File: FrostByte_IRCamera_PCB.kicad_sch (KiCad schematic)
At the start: 0 parts

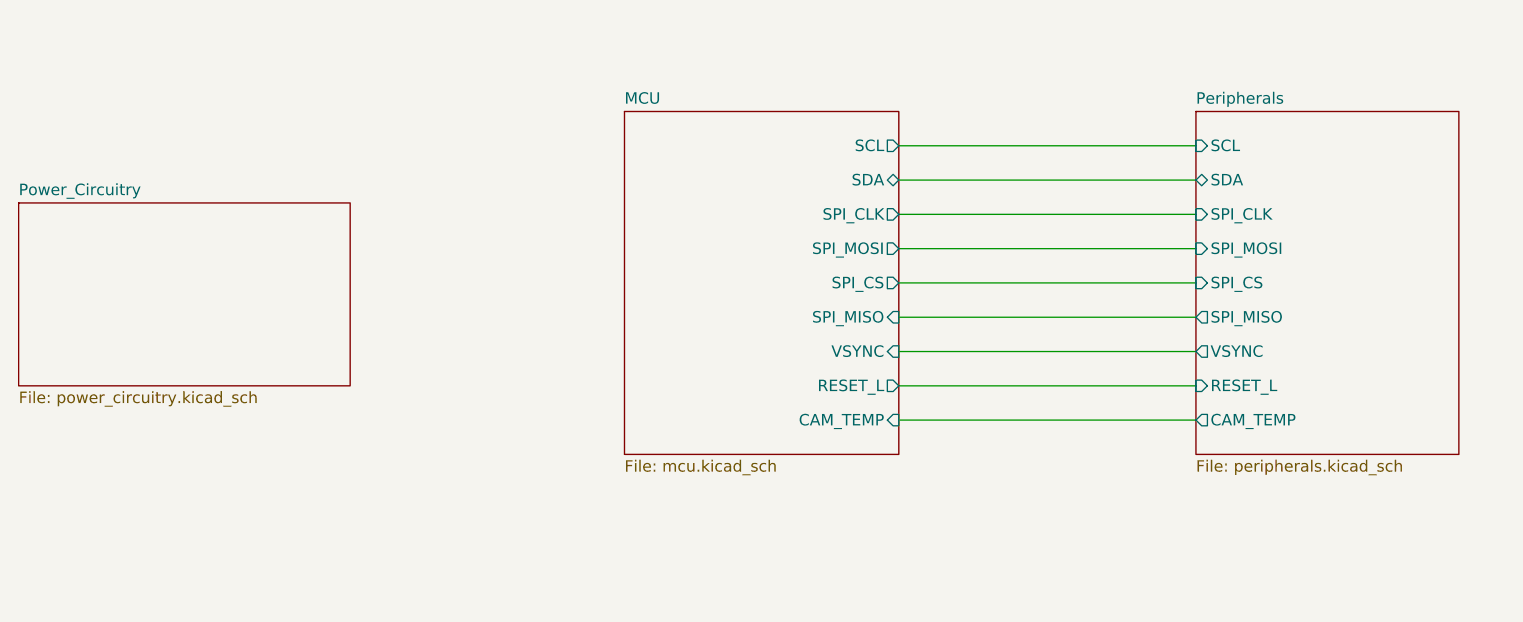
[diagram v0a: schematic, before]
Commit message: rev 2 added usb prog and i2c level shifting
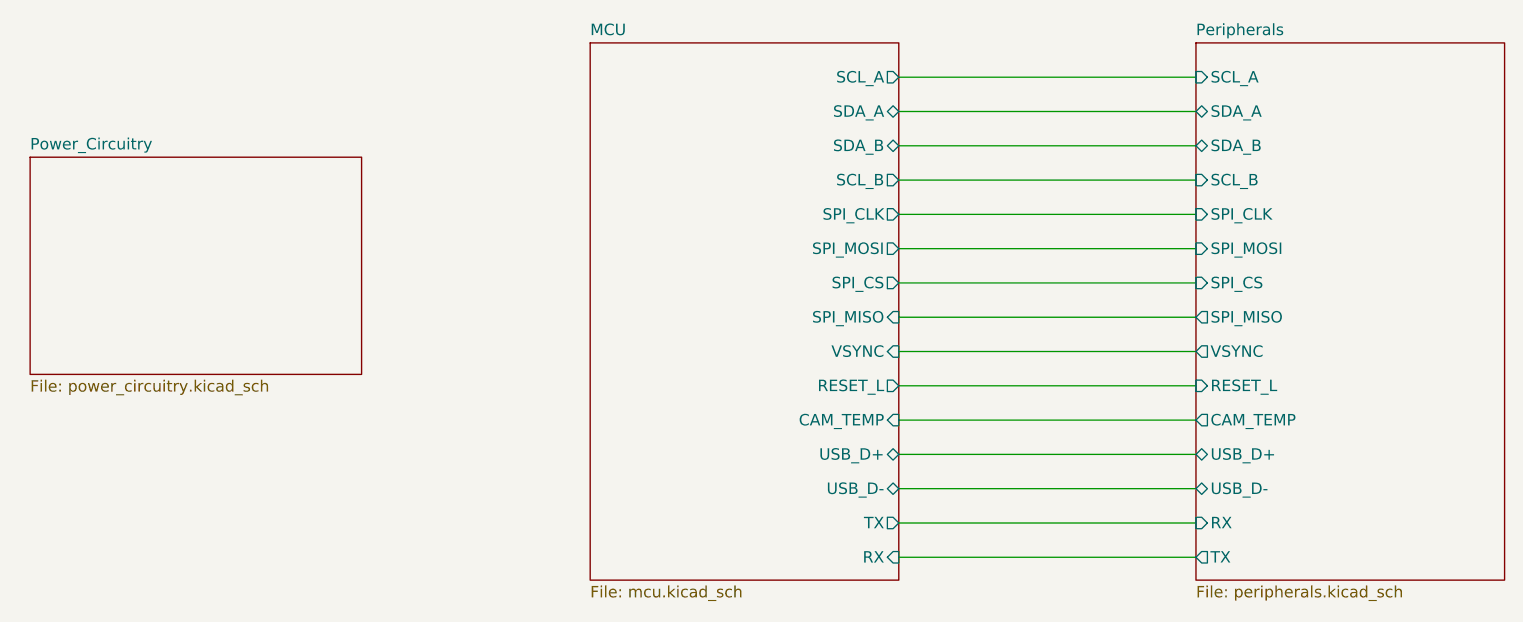
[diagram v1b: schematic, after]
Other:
- sheet MCU ports: added RX, SCL_A, SCL_B, SDA_A, SDA_B, TX, USB_D+, USB_D-; removed SCL, SDA
- sheet Peripherals ports: added RX, SCL_A, SCL_B, SDA_A, SDA_B, TX, USB_D+, USB_D-; removed SCL, SDA
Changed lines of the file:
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@@
+	(wire
+		(pts
+			(xy 162.56 76.2) (xy 195.58 76.2)
+		)
+		(stroke
+			(width 0)
+			(type default)
+		)
+	)
 	(wire
 		(pts
@@
 	(wire
 		(pts
+			(xy 162.56 114.3) (xy 195.58 114.3)
+		)
+		(stroke
+			(width 0)
+			(type default)
+		)
+	)
+	(wire
+		(pts
+			(xy 162.56 72.39) (xy 195.58 72.39)
+		)
+		(stroke
+			(width 0)
+			(type default)
+		)
+	)
+	(wire
+		(pts
 			(xy 162.56 87.63) (xy 195.58 87.63)
 		)
@@
 	(wire
 		(pts
+			(xy 162.56 125.73) (xy 195.58 125.73)
+		)
+		(stroke
+			(width 0)
+			(type default)
+		)
+	)
+	(wire
+		(pts
 			(xy 162.56 95.25) (xy 195.58 95.25)
 		)
@@
 		)
 	)
+	(wire
+		(pts
+			(xy 162.56 121.92) (xy 195.58 121.92)
+		)
+		(stroke
+			(width 0)
+			(type default)
+		)
+	)
+	(wire
+		(pts
+			(xy 162.56 118.11) (xy 195.58 118.11)
+		)
+		(stroke
+			(width 0)
+			(type default)
+		)
+	)
 	(sheet
-		(at 132.08 76.2)
-		(size 30.48 38.1)
+		(at 128.27 68.58)
+		(size 34.29 59.69)
 		(fields_autoplaced yes)
 		(stroke
@@
 		)
 		(property "Sheetname" "MCU"
-			(at 132.08 75.4884 0)
+			(at 128.27 67.8684 0)
 			(effects
 				(font
@@
 		)
 		(property "Sheetfile" "mcu.kicad_sch"
-			(at 132.08 114.8846 0)
+			(at 128.27 128.8546 0)
 			(effects
 				(font
@@
 			)
 		)
-		(pin "SCL" output
-			(at 162.56 80.01 0)
-			(effects
-				(font
-					(size 1.27 1.27)
-				)
-				(justify right)
-			)
-		)
-		(pin "SDA" bidirectional
-			(at 162.56 83.82 0)
-			(effects
-				(font
-					(size 1.27 1.27)
-				)
-				(justify right)
-			)
-		)
 		(pin "VSYNC" input
 			(at 162.56 102.87 0)
@@
 		(pin "SPI_MISO" input
 			(at 162.56 99.06 0)
+			(effects
+				(font
+					(size 1.27 1.27)
+				)
+				(justify right)
+			)
+		)
+		(pin "SCL_A" output
+			(at 162.56 72.39 0)
+			(effects
+				(font
+					(size 1.27 1.27)
+				)
+				(justify right)
+			)
+		)
+		(pin "SDA_A" bidirectional
+			(at 162.56 76.2 0)
+			(effects
+				(font
+					(size 1.27 1.27)
+				)
+				(justify right)
+			)
+		)
+		(pin "SDA_B" bidirectional
+			(at 162.56 80.01 0)
+			(effects
+				(font
+					(size 1.27 1.27)
+				)
+				(justify right)
+			)
+		)
+		(pin "SCL_B" output
+			(at 162.56 83.82 0)
+			(effects
+				(font
+					(size 1.27 1.27)
+				)
+				(justify right)
+			)
+		)
+		(pin "USB_D-" bidirectional
+			(at 162.56 118.11 0)
+			(effects
+				(font
+					(size 1.27 1.27)
+				)
+				(justify right)
+			)
+		)
+		(pin "USB_D+" bidirectional
+			(at 162.56 114.3 0)
+			(effects
+				(font
+					(size 1.27 1.27)
+				)
+				(justify right)
+			)
+		)
+		(pin "TX" output
+			(at 162.56 121.92 0)
+			(effects
+				(font
+					(size 1.27 1.27)
+				)
+				(justify right)
+			)
+		)
+		(pin "RX" input
+			(at 162.56 125.73 0)
 			(effects
 				(font
@@
 	)
 	(sheet
-		(at 195.58 76.2)
-		(size 29.21 38.1)
+		(at 195.58 68.58)
+		(size 34.29 59.69)
 		(fields_autoplaced yes)
 		(stroke
@@
 		)
 		(property "Sheetname" "Peripherals"
-			(at 195.58 75.4884 0)
+			(at 195.58 67.8684 0)
 			(effects
 				(font
@@
 		)
 		(property "Sheetfile" "peripherals.kicad_sch"
-			(at 195.58 114.8846 0)
+			(at 195.58 128.8546 0)
 			(effects
 				(font
@@
 			)
 		)
-		(pin "SCL" input
+		(pin "SCL_B" input
+			(at 195.58 83.82 180)
+			(effects
+				(font
+					(size 1.27 1.27)
+				)
+				(justify left)
+			)
+		)
+		(pin "SDA_B" bidirectional
 			(at 195.58 80.01 180)
 			(effects
@@
 			)
 		)
-		(pin "SDA" bidirectional
-			(at 195.58 83.82 180)
+		(pin "SCL_A" input
+			(at 195.58 72.39 180)
+			(effects
+				(font
+					(size 1.27 1.27)
+				)
+				(justify left)
+			)
+		)
+		(pin "SDA_A" bidirectional
+			(at 195.58 76.2 180)
+			(effects
+				(font
+					(size 1.27 1.27)
+				)
+				(justify left)
+			)
+		)
+		(pin "USB_D-" bidirectional
+			(at 195.58 118.11 180)
+			(effects
+				(font
+					(size 1.27 1.27)
+				)
+				(justify left)
+			)
+		)
+		(pin "USB_D+" bidirectional
+			(at 195.58 114.3 180)
+			(effects
+				(font
+					(size 1.27 1.27)
+				)
+				(justify left)
+			)
+		)
+		(pin "RX" input
+			(at 195.58 121.92 180)
+			(effects
+				(font
+					(size 1.27 1.27)
+				)
+				(justify left)
+			)
+		)
+		(pin "TX" output
+			(at 195.58 125.73 180)
 			(effects
 				(font
@@
 	)
 	(sheet
-		(at 64.77 86.36)
-		(size 36.83 20.32)
+		(at 66.04 81.28)
+		(size 36.83 24.13)
 		(fields_autoplaced yes)
 		(stroke
@@
 		)
 		(property "Sheetname" "Power_Circuitry"
-			(at 64.77 85.6484 0)
+			(at 66.04 80.5684 0)
 			(effects
 				(font
@@
 		)
 		(property "Sheetfile" "power_circuitry.kicad_sch"
-			(at 64.77 107.2646 0)
-			(effects
-				(font
+			(at 66.04 105.9946 0)
+			(effects
+				(font

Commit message: Rev A PCB Ordered
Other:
- company: (none) -> FrostByte Solutions
- title: (none) -> FrostByte IR Camera Interface Board
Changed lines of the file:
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@@
 	(generator_version "8.0")
 	(paper "A4")
+	(title_block
+		(title "FrostByte IR Camera Interface Board")
+		(company "FrostByte Solutions")
+		(comment 1 "Designed by Domenic Hampson")
+	)
 	(wire
 		(pts
